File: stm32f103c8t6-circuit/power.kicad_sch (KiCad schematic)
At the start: 7 parts, among them U3 HX9193-33GB

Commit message: Modify PCH and SCH
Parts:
- C13, C14, C15, C16: footprint PCM_001_GN_RCL_SMD:C0603(1608M) -> Capacitor_SMD:C_0603_1608Metric
- D4: value Diode_LED -> RED
- R8: footprint PCM_001_GN_RCL_SMD:R0603(1608M) -> ResistorSMD:R_0603_1608Metric
- U3: footprint PCM_003_GN_SMALL-SEMI_SMD:SOT-23-5 -> PackageSOT:SOT-23-5
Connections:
- net 5V renamed +5V
- net VCC renamed +3V3
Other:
- note added: "3V3_LED"
- note added: "LDC_3V3"
- moved on the sheet: C13, C14, C15, C16, D4, R8, U3

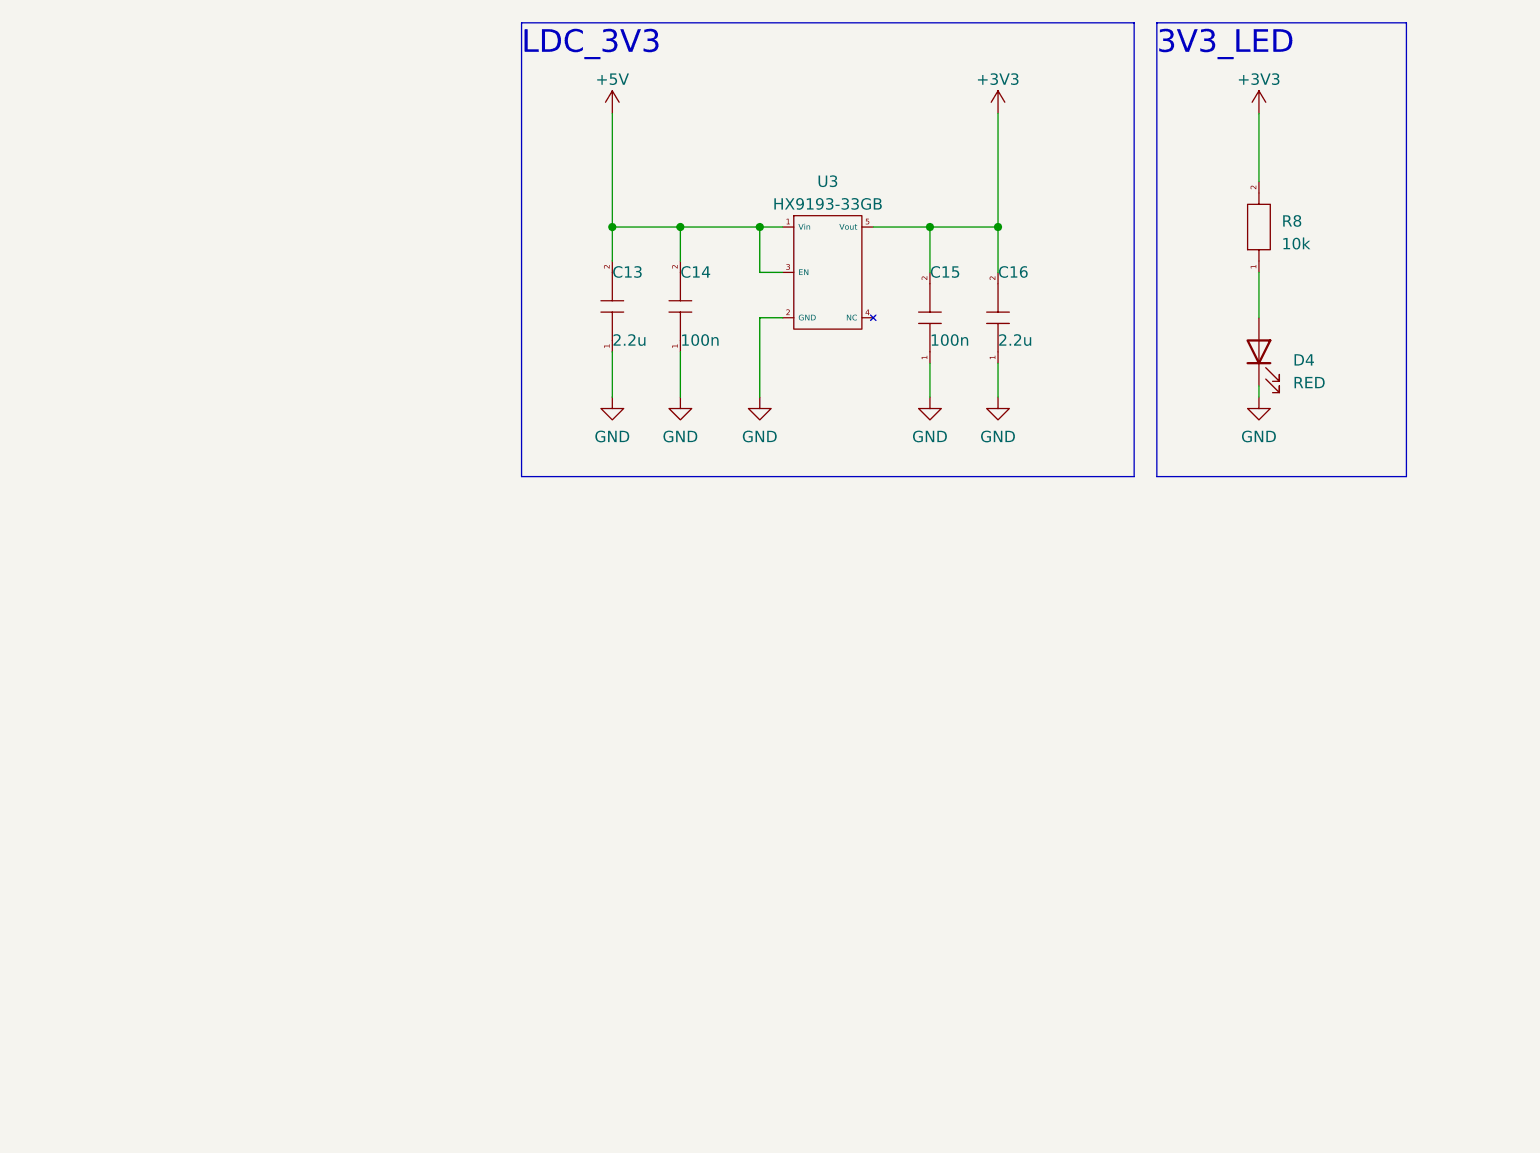
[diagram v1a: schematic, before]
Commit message: Fix some SCH bugs
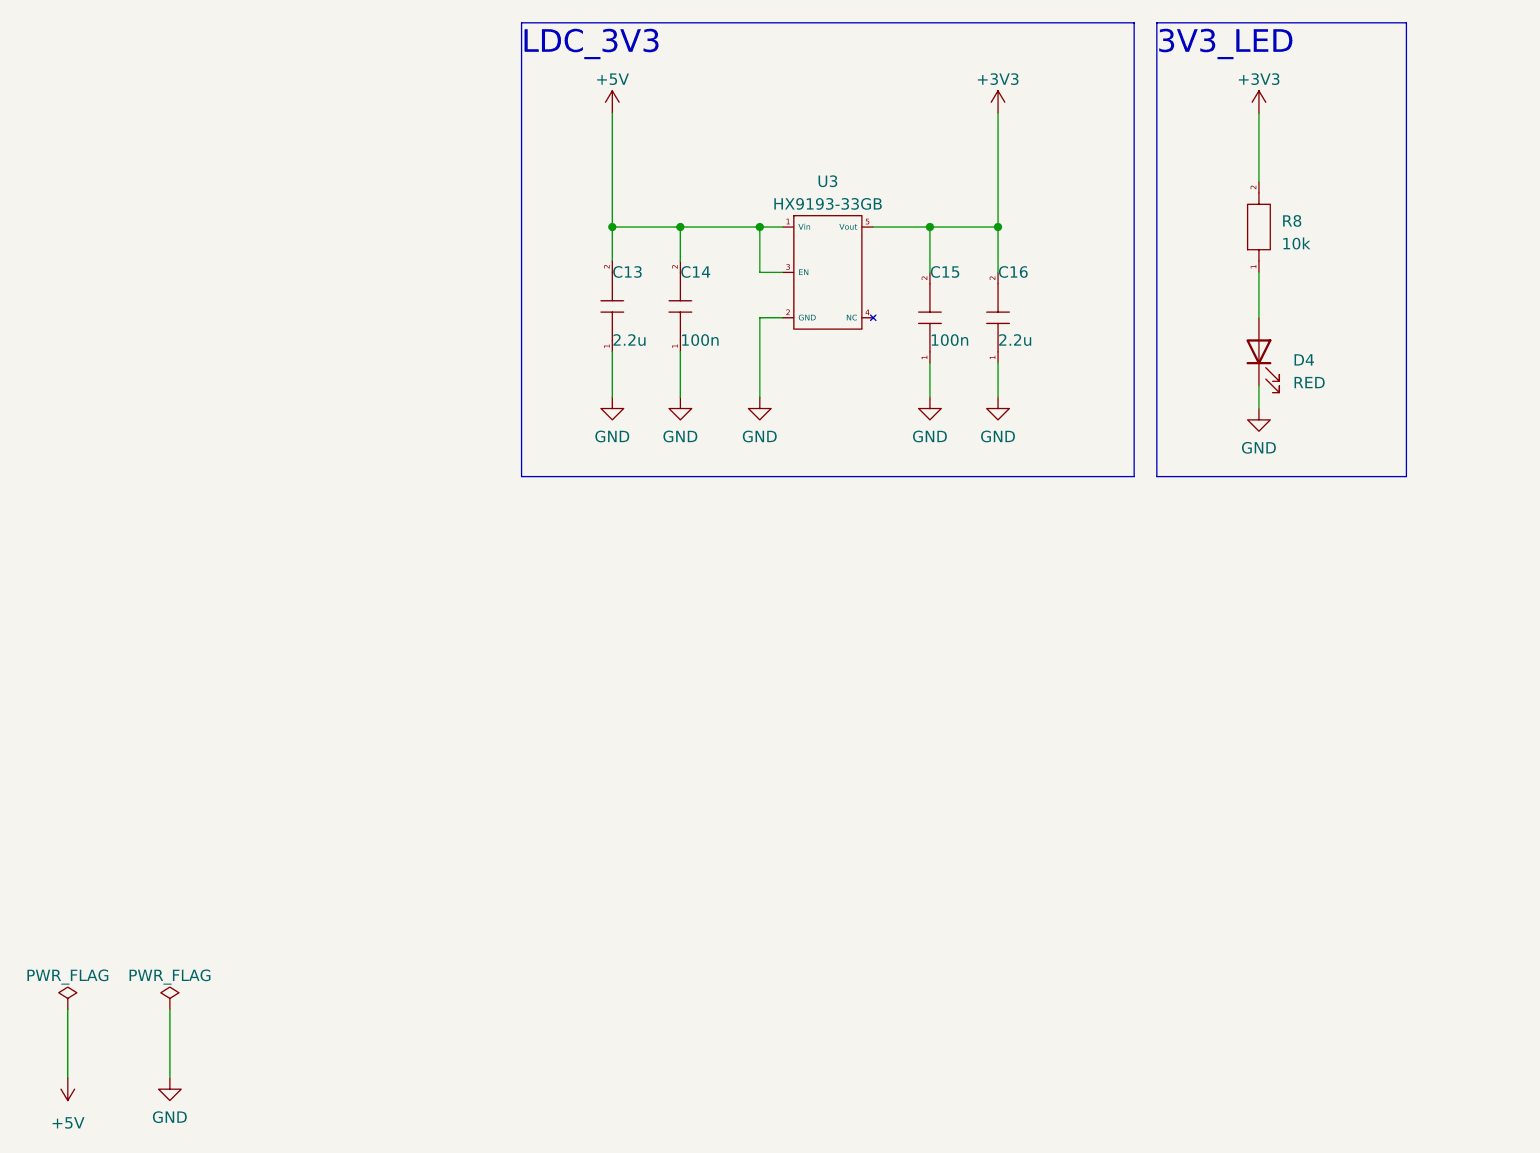
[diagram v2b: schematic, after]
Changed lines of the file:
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@@
+    (stroke (width 0) (type default))
+  )
+  (wire (pts (xy 26.67 173.99) (xy 26.67 181.61))
     (stroke (width 0) (type default))
   )
@@
     (stroke (width 0) (type default))
   )
+  (wire (pts (xy 38.1 173.99) (xy 38.1 181.61))
+    (stroke (width 0) (type default))
+  )
   (wire (pts (xy 130.81 101.6) (xy 130.81 105.41))
     (stroke (width 0) (type default))
@@
     (stroke (width 0) (type default))
   )
-  (wire (pts (xy 160.02 104.14) (xy 160.02 105.41))
+  (wire (pts (xy 160.02 104.14) (xy 160.02 106.68))
     (stroke (width 0) (type default))
   )
@@
     (effects (font (size 2.54 2.54)) (justify left bottom))
   )
+  (symbol (lib_id "power:+5V") (at 26.67 181.61 180) (unit 1)
+    (in_bom yes) (on_board yes) (dnp no) (fields_autoplaced)
+    (property "Reference" "#PWR058" (at 26.67 177.8 0)
+      (effects (font (size 1.27 1.27)) hide)
+    )
+    (property "Value" "+5V" (at 26.67 186.69 0)
+      (effects (font (size 1.27 1.27)))
+    )
+    (property "Footprint" "" (at 26.67 181.61 0)
+      (effects (font (size 1.27 1.27)) hide)
+    )
+    (property "Datasheet" "" (at 26.67 181.61 0)
+      (effects (font (size 1.27 1.27)) hide)
+    )
+    (pin "1")
+    (instances
+      (project "f103c8t6开发板"
+        (path "/74e35265-df09-4450-97d3-36a1cb5ad7a7/0a626b7b-053e-4ef0-baec-d548b065da00"
+          (reference "#PWR058") (unit 1)
+        )
+      )
+    )
+  )
   (symbol (lib_id "power:GND") (at 104.14 105.41 0) (unit 1)
     (in_bom yes) (on_board yes) (dnp no) (fields_autoplaced)
@@
         (path "/74e35265-df09-4450-97d3-36a1cb5ad7a7/0a626b7b-053e-4ef0-baec-d548b065da00"
           (reference "#PWR021") (unit 1)
+        )
+      )
+    )
+  )
+  (symbol (lib_id "power:PWR_FLAG") (at 38.1 173.99 0) (unit 1)
+    (in_bom yes) (on_board yes) (dnp no) (fields_autoplaced)
+    (property "Reference" "#FLG02" (at 38.1 172.085 0)
+      (effects (font (size 1.27 1.27)) hide)
+    )
+    (property "Value" "PWR_FLAG" (at 38.1 170.18 0)
+      (effects (font (size 1.27 1.27)))
+    )
+    (property "Footprint" "" (at 38.1 173.99 0)
+      (effects (font (size 1.27 1.27)) hide)
+    )
+    (property "Datasheet" "~" (at 38.1 173.99 0)
+      (effects (font (size 1.27 1.27)) hide)
+    )
+    (pin "1")
+    (instances
+      (project "f103c8t6开发板"
+        (path "/74e35265-df09-4450-97d3-36a1cb5ad7a7/0a626b7b-053e-4ef0-baec-d548b065da00"
+          (reference "#FLG02") (unit 1)
         )
       )
@@
     )
   )
+  (symbol (lib_id "power:PWR_FLAG") (at 26.67 173.99 0) (unit 1)
+    (in_bom yes) (on_board yes) (dnp no) (fields_autoplaced)
+    (property "Reference" "#FLG01" (at 26.67 172.085 0)
+      (effects (font (size 1.27 1.27)) hide)
+    )
+    (property "Value" "PWR_FLAG" (at 26.67 170.18 0)
+      (effects (font (size 1.27 1.27)))
+    )
+    (property "Footprint" "" (at 26.67 173.99 0)
+      (effects (font (size 1.27 1.27)) hide)
+    )
+    (property "Datasheet" "~" (at 26.67 173.99 0)
+      (effects (font (size 1.27 1.27)) hide)
+    )
+    (pin "1")
+    (instances
+      (project "f103c8t6开发板"
+        (path "/74e35265-df09-4450-97d3-36a1cb5ad7a7/0a626b7b-053e-4ef0-baec-d548b065da00"
+          (reference "#FLG01") (unit 1)
+        )
+      )
+    )
+  )
   (symbol (lib_id "001_Basic_PassiveComponents:001_Resistor") (at 160.02 86.36 90) (unit 1)
     (in_bom yes) (on_board yes) (dnp no) (fields_autoplaced)
@@
     )
   )
-  (symbol (lib_id "power:GND") (at 160.02 105.41 0) (unit 1)
-    (in_bom yes) (on_board yes) (dnp no) (fields_autoplaced)
-    (property "Reference" "#PWR027" (at 160.02 111.76 0)
-      (effects (font (size 1.27 1.27)) hide)
-    )
-    (property "Value" "GND" (at 160.02 109.855 0)
-      (effects (font (size 1.27 1.27)))
-    )
-    (property "Footprint" "" (at 160.02 105.41 0)
-      (effects (font (size 1.27 1.27)) hide)
-    )
-    (property "Datasheet" "" (at 160.02 105.41 0)
-      (effects (font (size 1.27 1.27)) hide)
-    )
+  (symbol (lib_id "power:GND") (at 38.1 181.61 0) (unit 1)
+    (in_bom yes) (on_board yes) (dnp no) (fields_autoplaced)
+    (property "Reference" "#PWR059" (at 38.1 187.96 0)
+      (effects (font (size 1.27 1.27)) hide)
+    )
+    (property "Value" "GND" (at 38.1 186.055 0)
+      (effects (font (size 1.27 1.27)))
+    )
+    (property "Footprint" "" (at 38.1 181.61 0)
+      (effects (font (size 1.27 1.27)) hide)
+    )
+    (property "Datasheet" "" (at 38.1 181.61 0)
+      (effects (font (size 1.27 1.27)) hide)
+    )
+    (pin "1")
+    (instances
+      (project "f103c8t6开发板"
+        (path "/74e35265-df09-4450-97d3-36a1cb5ad7a7/0a626b7b-053e-4ef0-baec-d548b065da00"
+          (reference "#PWR059") (unit 1)
+        )
+      )
+    )
+  )
+  (symbol (lib_id "power:GND") (at 160.02 106.68 0) (unit 1)
+    (in_bom yes) (on_board yes) (dnp no) (fields_autoplaced)
+    (property "Reference" "#PWR027" (at 160.02 113.03 0)
+      (effects (font (size 1.27 1.27)) hide)
+    )
+    (property "Value" "GND" (at 160.02 111.125 0)
+      (effects (font (size 1.27 1.27)))
+    )
+    (property "Footprint" "" (at 160.02 106.68 0)
+      (effects (font (size 1.27 1.27)) hide)
+    )
+    (property "Datasheet" "" (at 160.02 106.68 0)
+      (effects (font (size 1.27 1.27)) hide)
+    )
